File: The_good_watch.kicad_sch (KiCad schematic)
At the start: 52 parts, among them IC1 DW01A, J1 Main, J2 USB_C_Receptacle_USB2.0, J3 PROG, J4 Screen, J5 Button, J6 Conn_02x07_Counter_Clockwise, M1 Motor_DC, Q1 FS8205A, SW1 SW_Push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

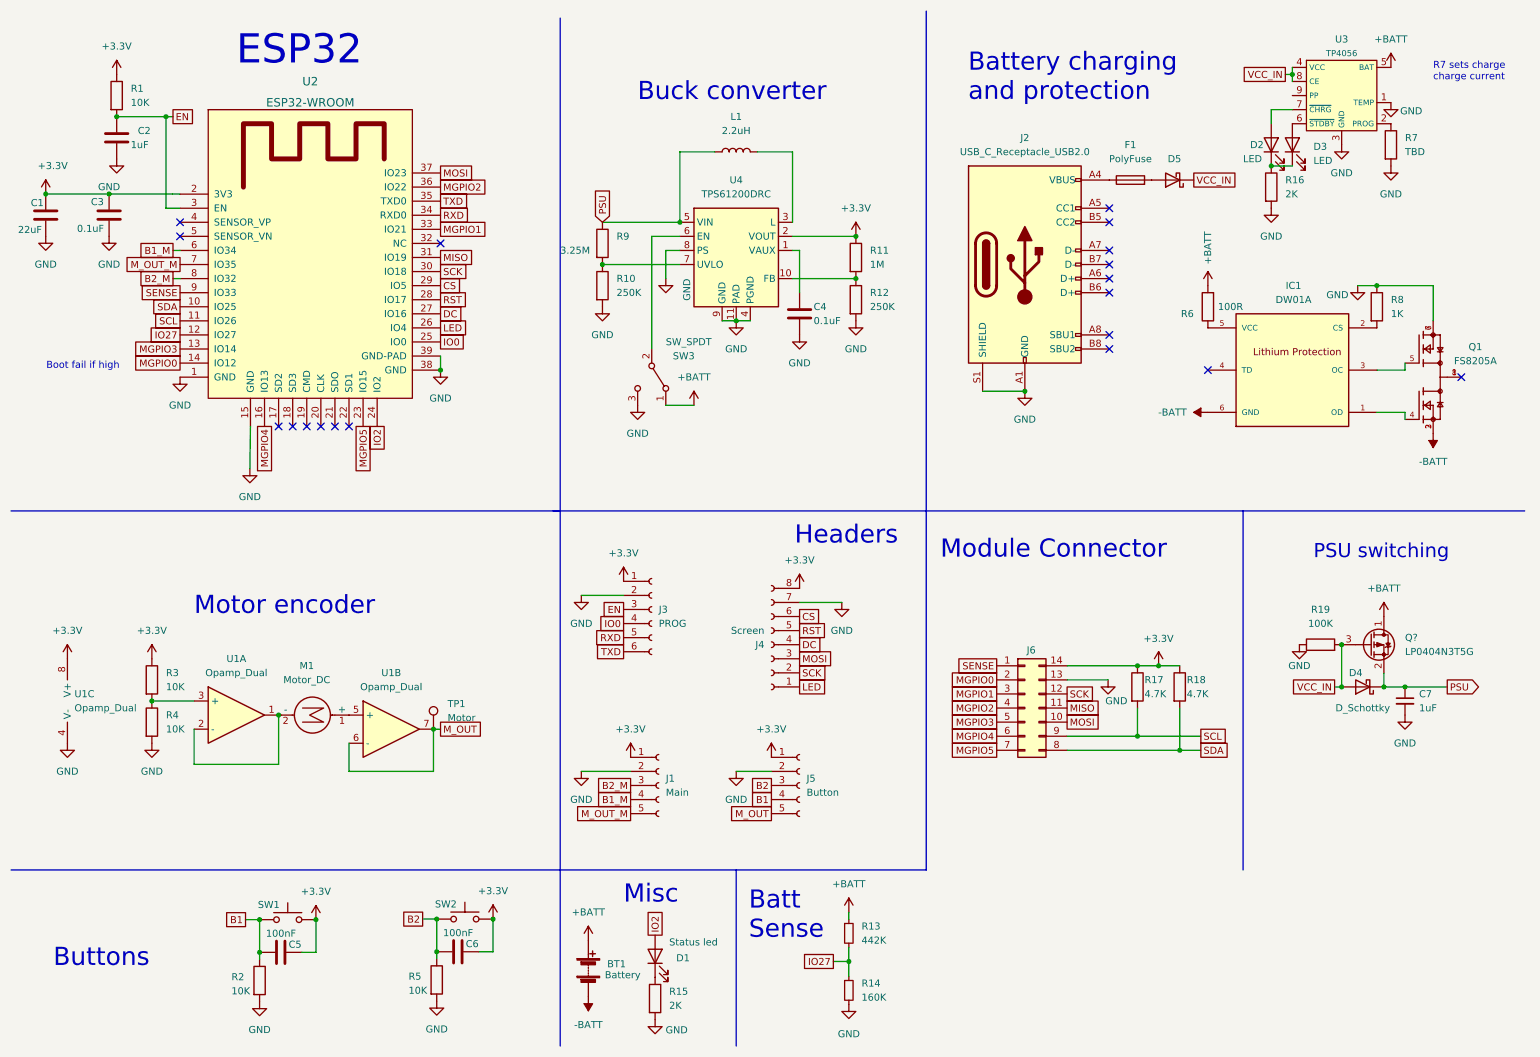
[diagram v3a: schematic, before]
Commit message: Changed power switch
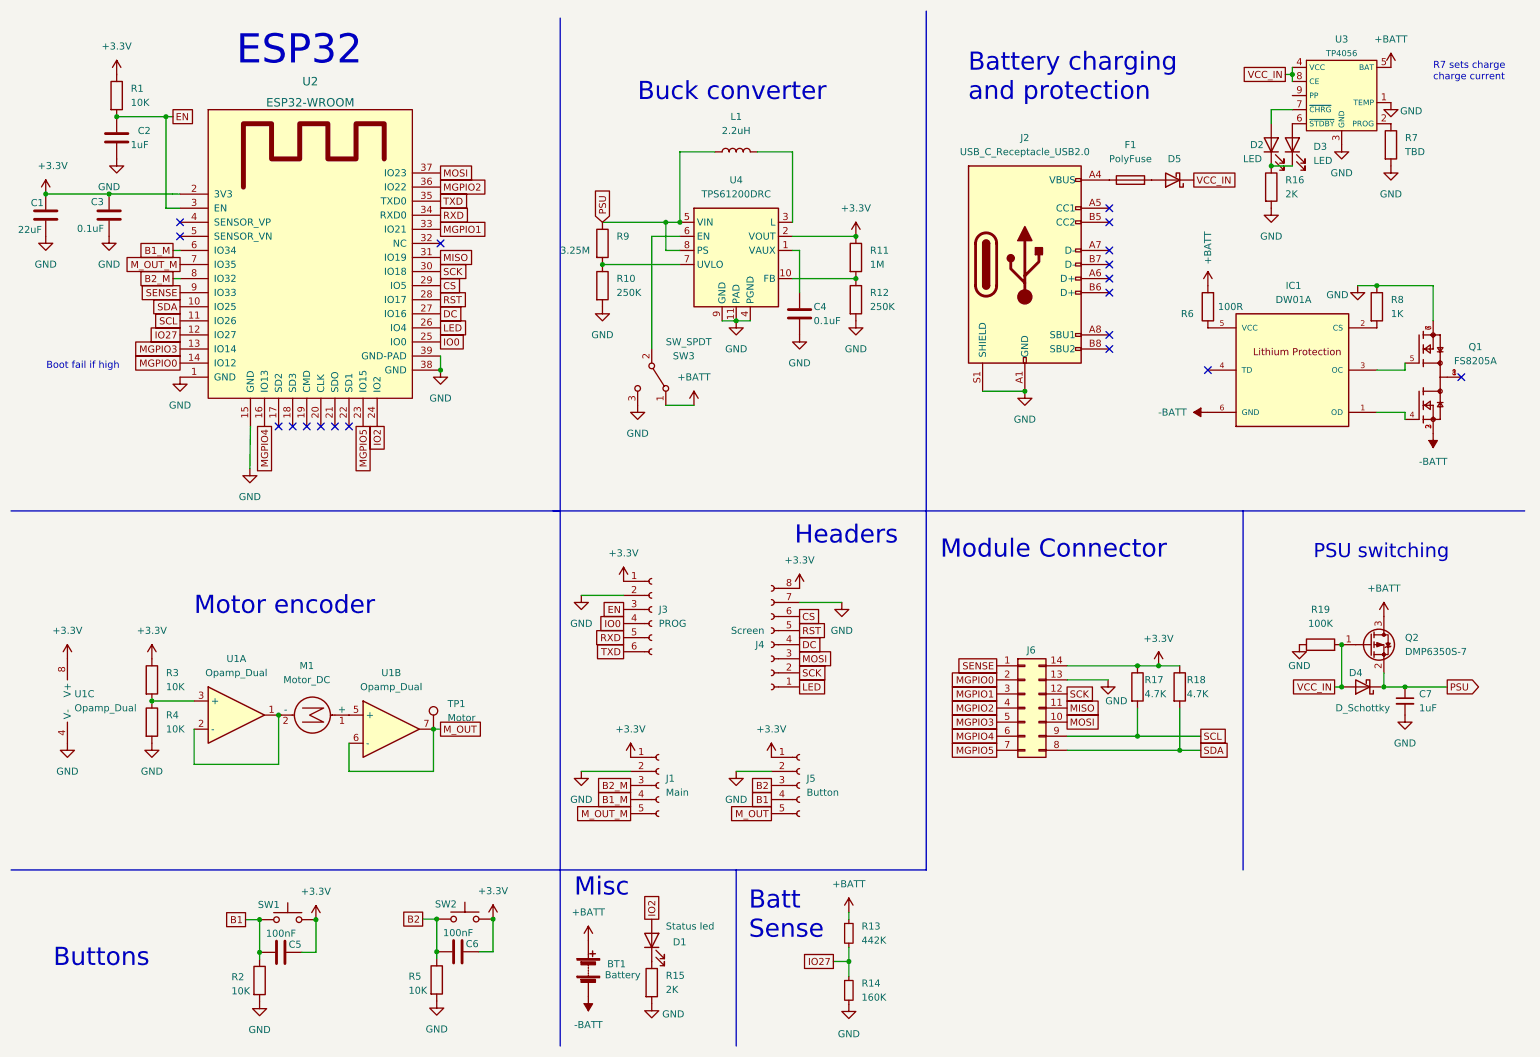
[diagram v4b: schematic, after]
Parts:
- removed Q?: LP0404N3T5G, symbol Device:Q_PMOS_DSG
- added Q2: DMP6350S-7, Package_TO_SOT_SMD:SOT-23, symbol Device:Q_PMOS_GSD
- SW3: footprint Connector_PinHeader_2.00mm:PinHeader_1x03_P2.00mm_Vertical -> Button_Switch_SMD:SW_SPDT_CK-JS102011SAQN
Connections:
- net +BATT: now also Q2.3 (D)
- net GND: no longer U4.8 (PS)
- net PSU: now also U4.8 (PS), Q2.2 (S)
- net VCC_IN: now also Q2.1 (G)
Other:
- moved on the sheet: D1, R15
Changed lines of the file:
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@@
   (junction (at 222.25 144.78) (diameter 0) (color 0 0 0 0)
   )
+  (junction (at 251.46 125.73) (diameter 0) (color 0 0 0 0)
+  )
   (junction (at 36.83 135.89) (diameter 0) (color 0 0 0 0)
   )
@@
   (junction (at 88.2142 175.2346) (diameter 0) (color 0 0 0 0)
   )
+  (junction (at 129.54 49.53) (diameter 0) (color 0 0 0 0)
+  )
   (junction (at 66.421 175.3362) (diameter 0) (color 0 0 0 0)
   )
@@
   (junction (at 88.2142 181.1274) (diameter 0) (color 0 0 0 0)
   )
-  (junction (at 251.46 125.73) (diameter 0) (color 0 0 0 0)
-  )
   (junction (at 59.69 138.43) (diameter 0) (color 0 0 0 0)
   )
@@
     (stroke (width 0) (type default) (color 0 0 0 0))
   )
+  (wire (pts (xy 129.54 49.53) (xy 129.54 54.61))
+    (stroke (width 0) (type default) (color 0 0 0 0))
+  )
   (wire (pts (xy 132.08 49.53) (xy 132.08 36.83))
     (stroke (width 0) (type default) (color 0 0 0 0))
@@
     (stroke (width 0) (type default) (color 0 0 0 0))
   )
-  (wire (pts (xy 118.11 49.53) (xy 132.08 49.53))
+  (wire (pts (xy 118.11 49.53) (xy 129.54 49.53))
     (stroke (width 0) (type default) (color 0 0 0 0))
   )
@@
     (stroke (width 0) (type default) (color 0 0 0 0))
   )
-  (wire (pts (xy 129.54 54.61) (xy 129.54 59.69))
-    (stroke (width 0) (type default) (color 0 0 0 0))
-  )
   (wire (pts (xy 152.4 54.61) (xy 153.67 54.61))
     (stroke (width 0) (type default) (color 0 0 0 0))
@@
     (stroke (width 0) (type default) (color 0 0 0 0))
   )
+  (wire (pts (xy 129.54 49.53) (xy 132.08 49.53))
+    (stroke (width 0) (type default) (color 0 0 0 0))
+  )
   (wire (pts (xy 88.2142 182.3974) (xy 88.2142 181.1274))
     (stroke (width 0) (type default) (color 0 0 0 0))
@@
     (effects (font (size 3.27 3.27)) (justify right bottom))
   )
-  (text "Misc\n" (at 121.92 172.72 0)
+  (text "Misc\n" (at 113.03 171.45 0)
     (effects (font (size 3.27 3.27)) (justify left bottom))
   )
@@
     )
   )
-  (global_label "IO2" (shape passive) (at 127.6096 178.1302 90) (fields_autoplaced)
+  (global_label "IO2" (shape passive) (at 127 175.26 90) (fields_autoplaced)
     (effects (font (size 1.27 1.27)) (justify left))
-    (property "Intersheet References" "${INTERSHEET_REFS}" (id 0) (at 127.5302 172.5723 90)
+    (property "Intersheet References" "${INTERSHEET_REFS}" (id 0) (at 126.9206 169.7021 90)
       (effects (font (size 1.27 1.27)) (justify left) hide)
     )
@@
       (effects (font (size 1.27 1.27)) (justify left))
     )
-    (property "Footprint" "Connector_PinHeader_2.00mm:PinHeader_1x03_P2.00mm_Vertical" (id 2) (at 127 77.47 0)
+    (property "Footprint" "Button_Switch_SMD:SW_SPDT_CK-JS102011SAQN" (id 2) (at 127 77.47 0)
       (effects (font (size 1.27 1.27)) hide)
     )
@@
     (pin "5")
   )
-  (symbol (lib_id "Device:Q_PMOS_DSG") (at 256.54 125.73 0) (unit 1)
-    (in_bom yes) (on_board yes) (fields_autoplaced)
-    (property "Reference" "Q?" (id 0) (at 262.89 124.4599 0)
-      (effects (font (size 1.27 1.27)) (justify left))
-    )
-    (property "Value" "LP0404N3T5G" (id 1) (at 262.89 126.9999 0)
-      (effects (font (size 1.27 1.27)) (justify left))
-    )
-    (property "Footprint" "" (id 2) (at 261.62 123.19 0)
-      (effects (font (size 1.27 1.27)) hide)
-    )
-    (property "Datasheet" "~" (id 3) (at 256.54 125.73 0)
-      (effects (font (size 1.27 1.27)) hide)
-    )
-    (pin "1")
-    (pin "2")
-    (pin "3")
-  )
   (symbol (lib_id "power:GND") (at 114.3 116.84 0) (unit 1)
     (in_bom yes) (on_board yes) (fields_autoplaced)
@@
     (pin "1")
   )
-  (symbol (lib_id "Device:LED") (at 127.6096 181.9402 90) (unit 1)
+  (symbol (lib_id "Device:LED") (at 127 179.07 90) (unit 1)
     (in_bom yes) (on_board yes)
-    (property "Reference" "D1" (id 0) (at 131.4196 182.2576 90)
+    (property "Reference" "D1" (id 0) (at 130.81 179.3874 90)
       (effects (font (size 1.27 1.27)) (justify right))
     )
-    (property "Value" "Status led" (id 1) (at 130.1496 179.4002 90)
+    (property "Value" "Status led" (id 1) (at 129.54 176.53 90)
       (effects (font (size 1.27 1.27)) (justify right))
     )
-    (property "Footprint" "LED_SMD:LED_0603_1608Metric_Pad1.05x0.95mm_HandSolder" (id 2) (at 127.6096 181.9402 0)
+    (property "Footprint" "LED_SMD:LED_0603_1608Metric_Pad1.05x0.95mm_HandSolder" (id 2) (at 127 179.07 0)
       (effects (font (size 1.27 1.27)) hide)
     )
-    (property "Datasheet" "~" (id 3) (at 127.6096 181.9402 0)
+    (property "Datasheet" "~" (id 3) (at 127 179.07 0)
       (effects (font (size 1.27 1.27)) hide)
     )
@@
     (pin "8")
   )
-  (symbol (lib_id "power:GND") (at 129.54 59.69 0) (unit 1)
-    (in_bom yes) (on_board yes)
-    (property "Reference" "#PWR0138" (id 0) (at 129.54 66.04 0)
-      (effects (font (size 1.27 1.27)) hide)
-    )
-    (property "Value" "GND" (id 1) (at 133.35 59.69 90)
-      (effects (font (size 1.27 1.27)) (justify right))
-    )
-    (property "Footprint" "" (id 2) (at 129.54 59.69 0)
-      (effects (font (size 1.27 1.27)) hide)
-    )
-    (property "Datasheet" "" (id 3) (at 129.54 59.69 0)
-      (effects (font (size 1.27 1.27)) hide)
-    )
-    (pin "1")
-  )
   (symbol (lib_id "power:+3.3V") (at 66.421 175.3362 0) (unit 1)
     (in_bom yes) (on_board yes) (fields_autoplaced)
@@
     (pin "2")
   )
-  (symbol (lib_id "Device:R") (at 127.6096 189.5602 0) (unit 1)
+  (symbol (lib_id "Device:Q_PMOS_GSD") (at 256.54 125.73 0) (unit 1)
     (in_bom yes) (on_board yes) (fields_autoplaced)
-    (property "Reference" "R15" (id 0) (at 130.1496 188.2901 0)
+    (property "Reference" "Q2" (id 0) (at 262.89 124.4599 0)
       (effects (font (size 1.27 1.27)) (justify left))
     )
-    (property "Value" "2K" (id 1) (at 130.1496 190.8301 0)
+    (property "Value" "DMP6350S-7" (id 1) (at 262.89 126.9999 0)
       (effects (font (size 1.27 1.27)) (justify left))
     )
-    (property "Footprint" "Resistor_SMD:R_0805_2012Metric" (id 2) (at 125.8316 189.5602 90)
+    (property "Footprint" "Package_TO_SOT_SMD:SOT-23" (id 2) (at 261.62 123.19 0)
       (effects (font (size 1.27 1.27)) hide)
     )
-    (property "Datasheet" "~" (id 3) (at 127.6096 189.5602 0)
+    (property "Datasheet" "~" (id 3) (at 256.54 125.73 0)
+      (effects (font (size 1.27 1.27)) hide)
+    )
+    (pin "1")
+    (pin "2")
+    (pin "3")
+  )
+  (symbol (lib_id "Device:R") (at 127 186.69 0) (unit 1)
+    (in_bom yes) (on_board yes) (fields_autoplaced)
+    (property "Reference" "R15" (id 0) (at 129.54 185.4199 0)
+      (effects (font (size 1.27 1.27)) (justify left))
+    )
+    (property "Value" "2K" (id 1) (at 129.54 187.9599 0)
+      (effects (font (size 1.27 1.27)) (justify left))
+    )
+    (property "Footprint" "Resistor_SMD:R_0805_2012Metric" (id 2) (at 125.222 186.69 90)
+      (effects (font (size 1.27 1.27)) hide)
+    )
+    (property "Datasheet" "~" (id 3) (at 127 186.69 0)
       (effects (font (size 1.27 1.27)) hide)
     )
@@
     (pin "2")
   )
-  (symbol (lib_id "power:GND") (at 127.6096 193.3702 0) (unit 1)
+  (symbol (lib_id "power:GND") (at 127 190.5 0) (unit 1)
     (in_bom yes) (on_board yes)
-    (property "Reference" "#PWR0116" (id 0) (at 127.6096 199.7202 0)
+    (property "Reference" "#PWR0116" (id 0) (at 127 196.85 0)
       (effects (font (size 1.27 1.27)) hide)
     )
-    (property "Value" "GND" (id 1) (at 131.4958 195.2498 0))
-    (property "Footprint" "" (id 2) (at 127.6096 193.3702 0)
+    (property "Value" "GND" (id 1) (at 130.8862 192.3796 0))
+    (property "Footprint" "" (id 2) (at 127 190.5 0)
       (effects (font (size 1.27 1.27)) hide)
     )
-    (property "Datasheet" "" (id 3) (at 127.6096 193.3702 0)
+    (property "Datasheet" "" (id 3) (at 127 190.5 0)
       (effects (font (size 1.27 1.27)) hide)
     )
@@
       (reference "#PWR0137") (unit 1) (value "+BATT") (footprint "")
     )
-    (path "/36b5cb7e-6b9b-4ba8-b494-07bdd9971ac6"
-      (reference "#PWR0138") (unit 1) (value "GND") (footprint "")
-    )
     (path "/e26c0f02-abc5-4023-8465-3797f6d41374"
       (reference "#PWR0139") (unit 1) (value "GND") (footprint "")
@@
       (reference "Q1") (unit 1) (value "FS8205A") (footprint "FS8205A:SOP65P640X120-8N")
     )
-    (path "/25ce492d-5fce-4cd7-9136-dc23b5145044"
-      (reference "Q?") (unit 1) (value "LP0404N3T5G") (footprint "")
+    (path "/92475262-716c-4a4e-bbfb-f4267d0cd7ff"
+      (reference "Q2") (unit 1) (value "DMP6350S-7") (footprint "Package_TO_SOT_SMD:SOT-23")
     )
     (path "/c224661f-9b65-4914-ba8e-266913ab43a5"
@@
     )
     (path "/23f38011-59d9-4f99-a045-c97ad7dbc6c8"
-      (reference "SW3") (unit 1) (value "SW_SPDT") (footprint "Connector_PinHeader_2.00mm:PinHeader_1x03_P2.00mm_Vertical")
+      (reference "SW3") (unit 1) (value "SW_SPDT") (footprint "Button_Switch_SMD:SW_SPDT_CK-JS102011SAQN")
     )
     (path "/f420c2c9-a52b-4ad4-85c4-5b6adc3d9df3"
